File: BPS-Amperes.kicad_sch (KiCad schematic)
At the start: 46 parts, among them J1 ShuntConn, J2 LeaderConn, J3 Conn_01x04, U1 INA186A3IDDFT, U2 RO-123.3S_HP, U3 LTC6820, U4 HX1188FNL, U5 REF1930AIDDCT, U6 LTC2315, U7 OPA2196

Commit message: Minor fixing
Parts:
- D1: symbol Device:LED_ALT -> Device:LED
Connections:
- net GND: now also D1.1 (K)
- net at R2.2: now also D1.2 (A)
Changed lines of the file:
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@@
     (pin "2")
   )
-  (symbol (lib_id "Device:LED_ALT") (at 121.92 57.15 90) (unit 1)
+  (symbol (lib_id "Device:LED") (at 121.92 57.15 90) (unit 1)
     (in_bom yes) (on_board yes)
     (property "Reference" "D1" (id 0) (at 124.9172 56.1594 90)
@@
       (effects (font (size 1.27 1.27)) hide)
     )
+    (pin "1")
+    (pin "2")
   )
   (symbol (lib_id "power:GNDPWR") (at 40.64 60.96 0) (unit 1)

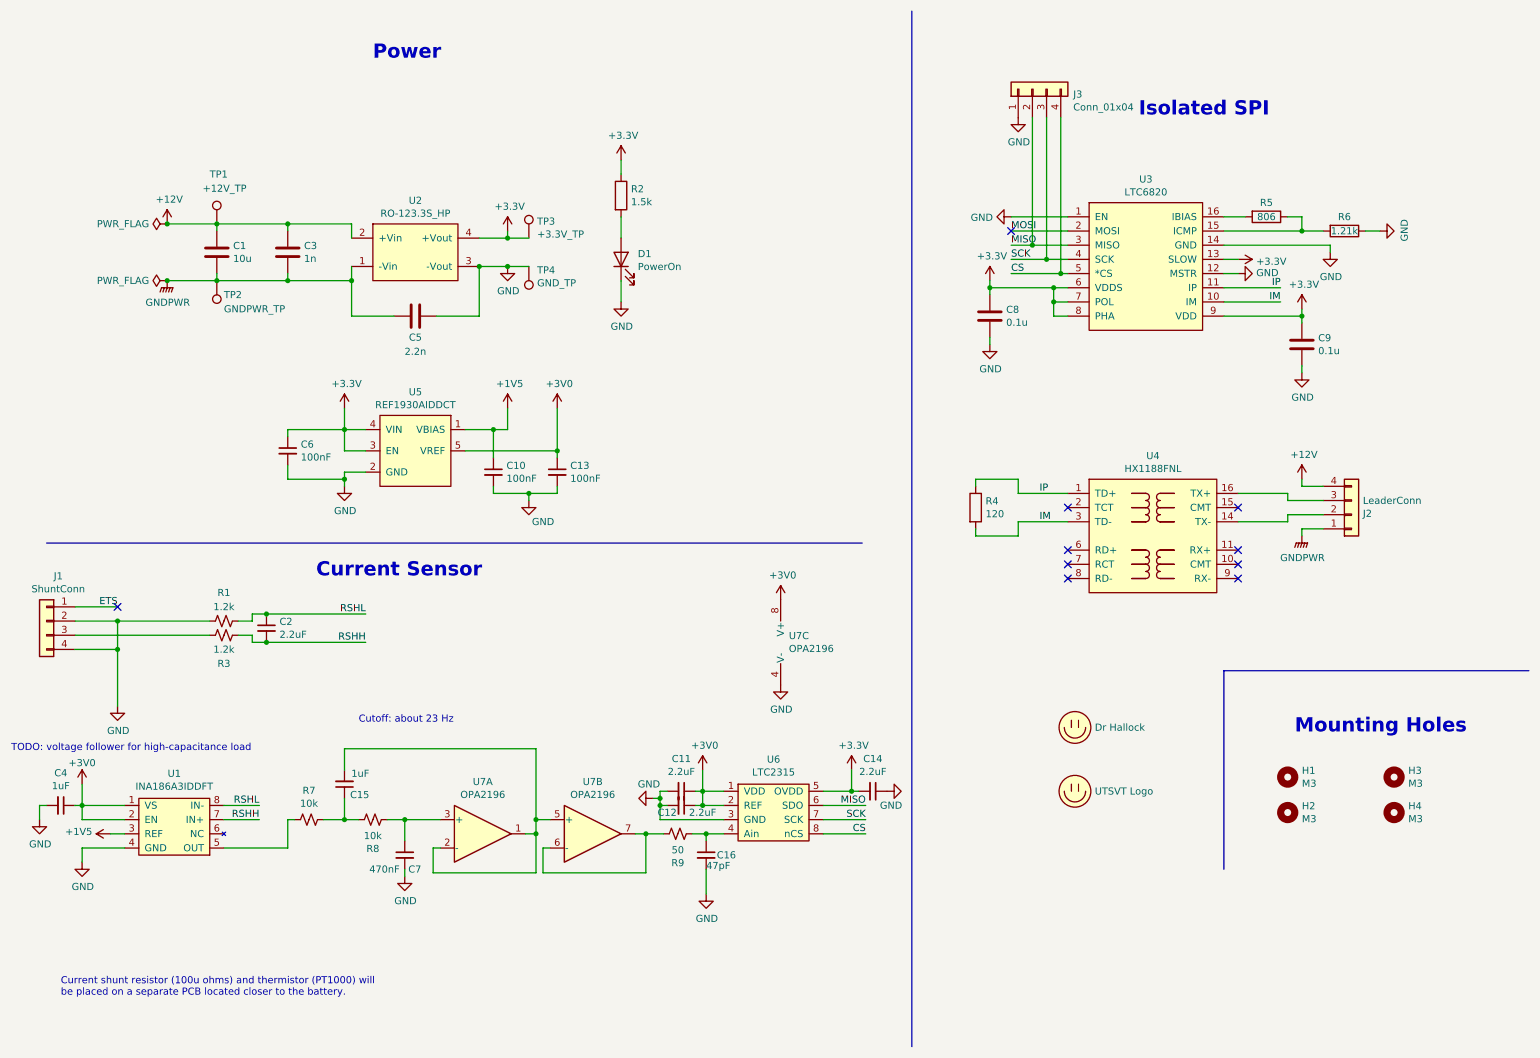
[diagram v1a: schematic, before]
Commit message: emi + reverse polarity + analog overvolt protection
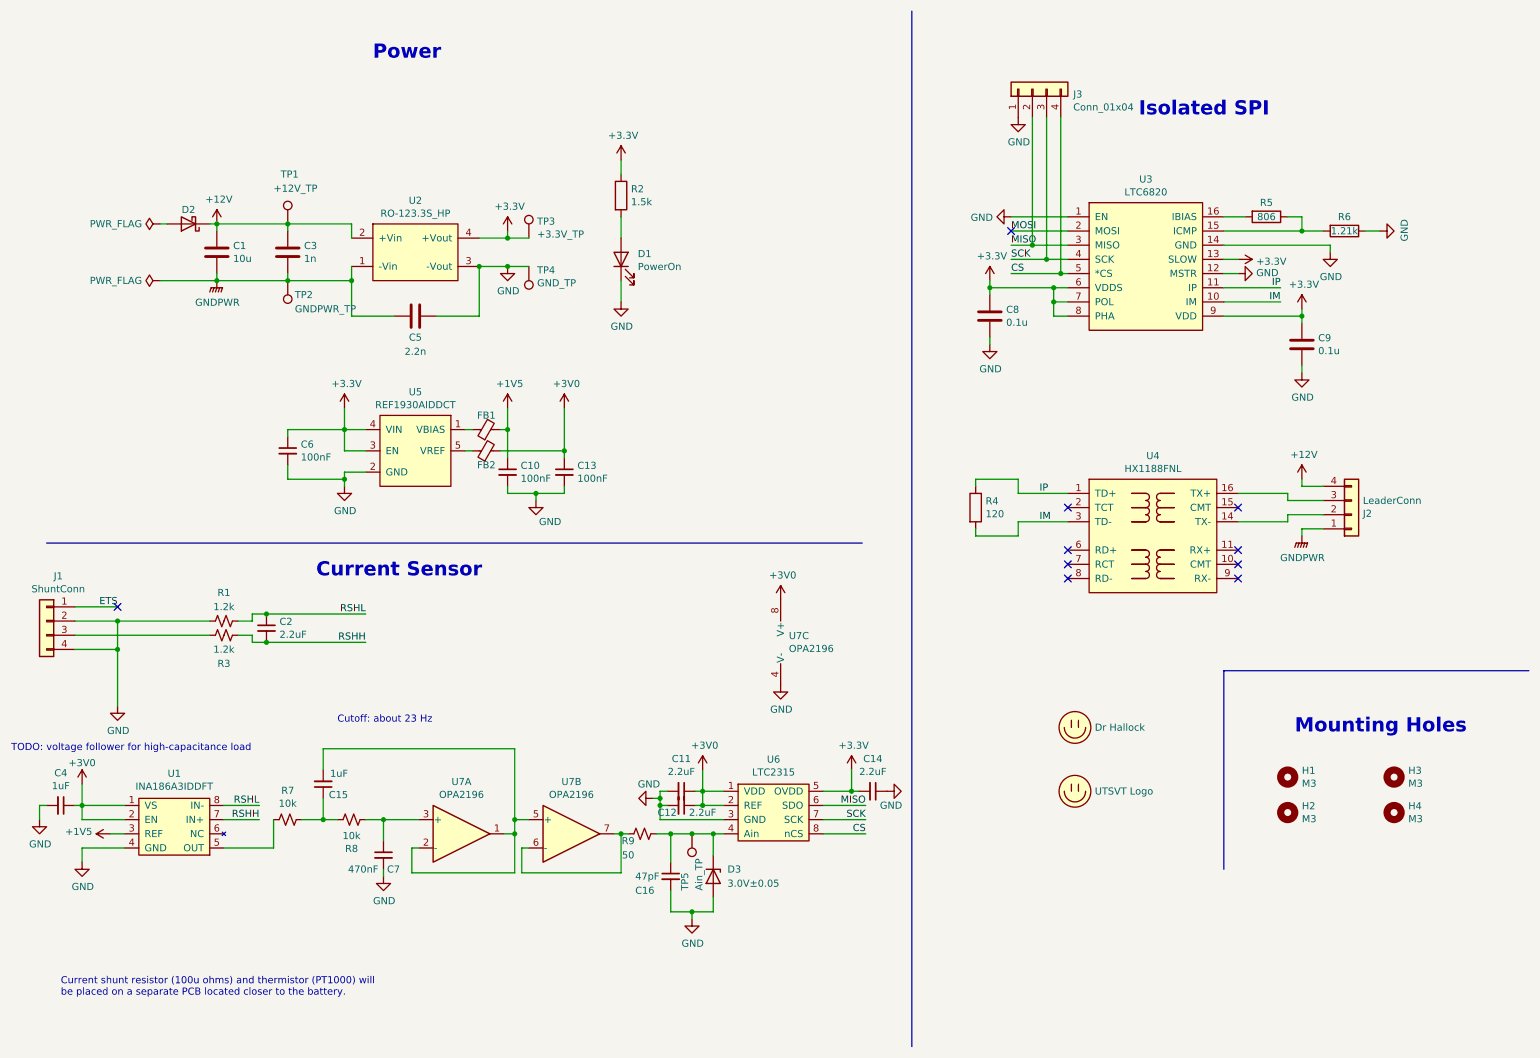
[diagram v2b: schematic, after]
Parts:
- added D2: D_Schottky, symbol Device:D_Schottky
- added D3: 3.0V±0.05, symbol Device:D_Zener
- added FB1, FB2: FerriteBead_Small, symbol Device:FerriteBead_Small
- added TP5: Ain_TP, symbol Connector:TestPoint
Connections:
- net +12V: now also D2.1 (K)
- net +1V5: now also FB1.2; no longer U5.1 (VBIAS)
- net +3V0: now also FB2.2; no longer U5.5 (VREF)
- net GND: now also D3.2 (A)
- net at C16.1, R9.2, U6.4 (Ain): now also D3.1 (K), TP5.1
- new net: FB1.1, U5.1 (VBIAS)
- new net: FB2.1, U5.5 (VREF)
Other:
- moved on the sheet: C10, C13, C15, C16, C7, R7, R8, R9, TP1, TP2, U7A, U7B

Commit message: hat connector
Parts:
- J1: symbol Connector_Generic:Conn_01x04 -> Connector_Generic:Conn_01x05
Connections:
- net +3V3: now also J1.4 (Pin_4)
- net GND: now also J1.5 (Pin_5); no longer J1.4 (Pin_4)

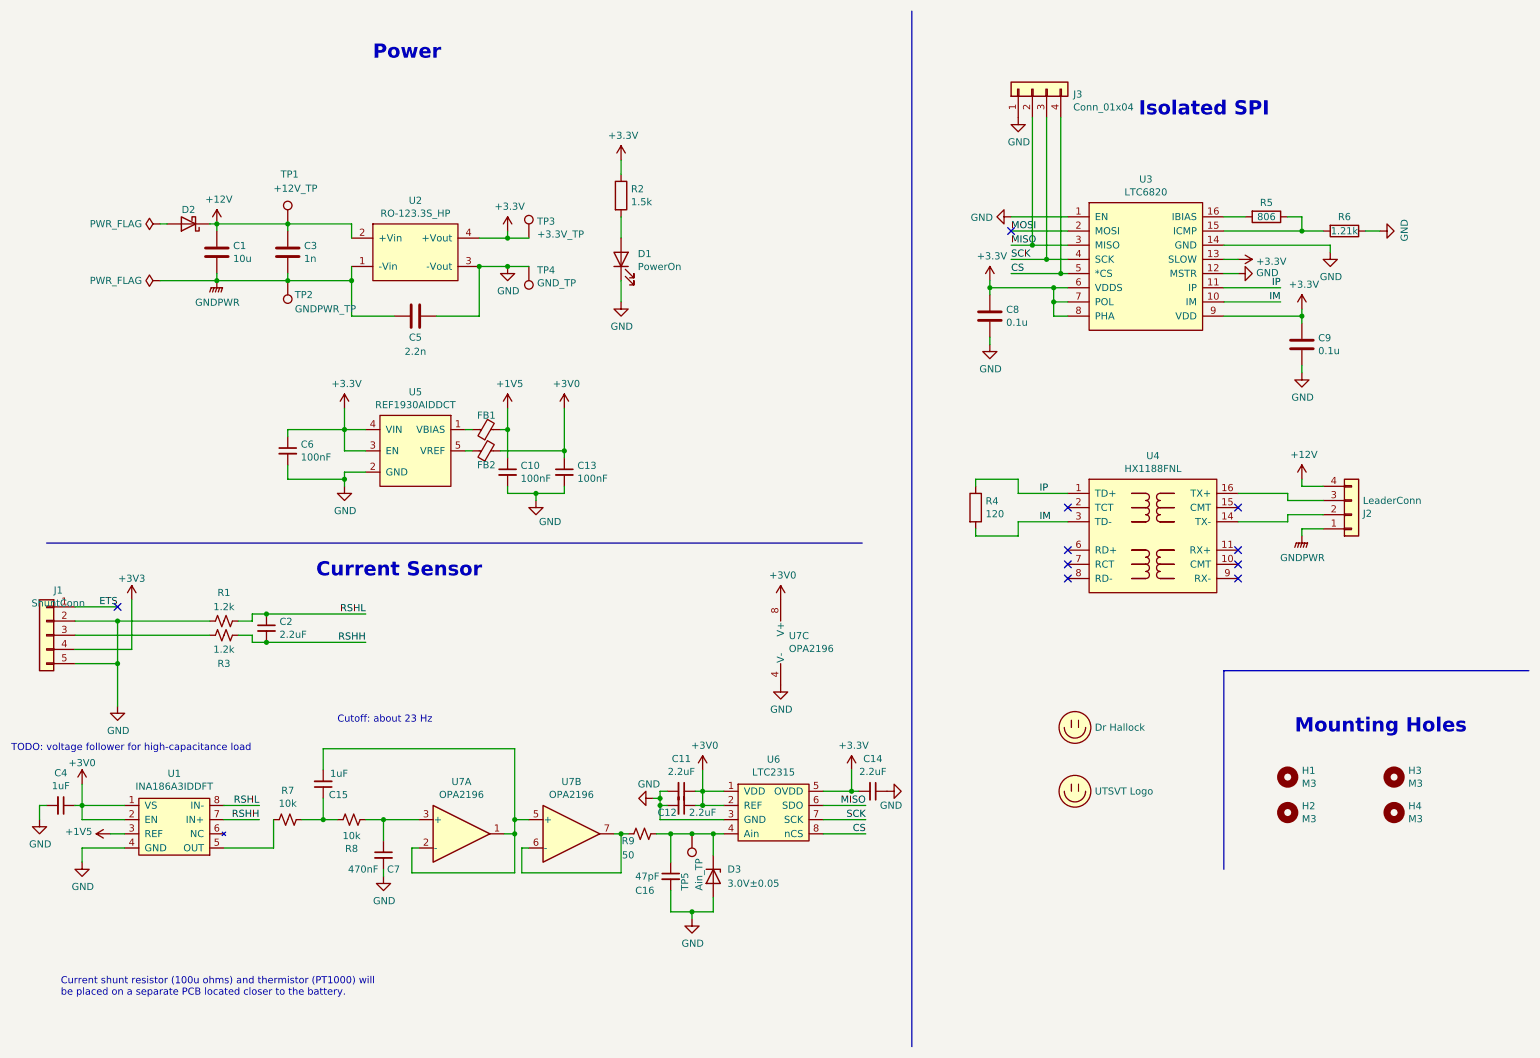
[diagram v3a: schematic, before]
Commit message: more bypass caps and other fixes
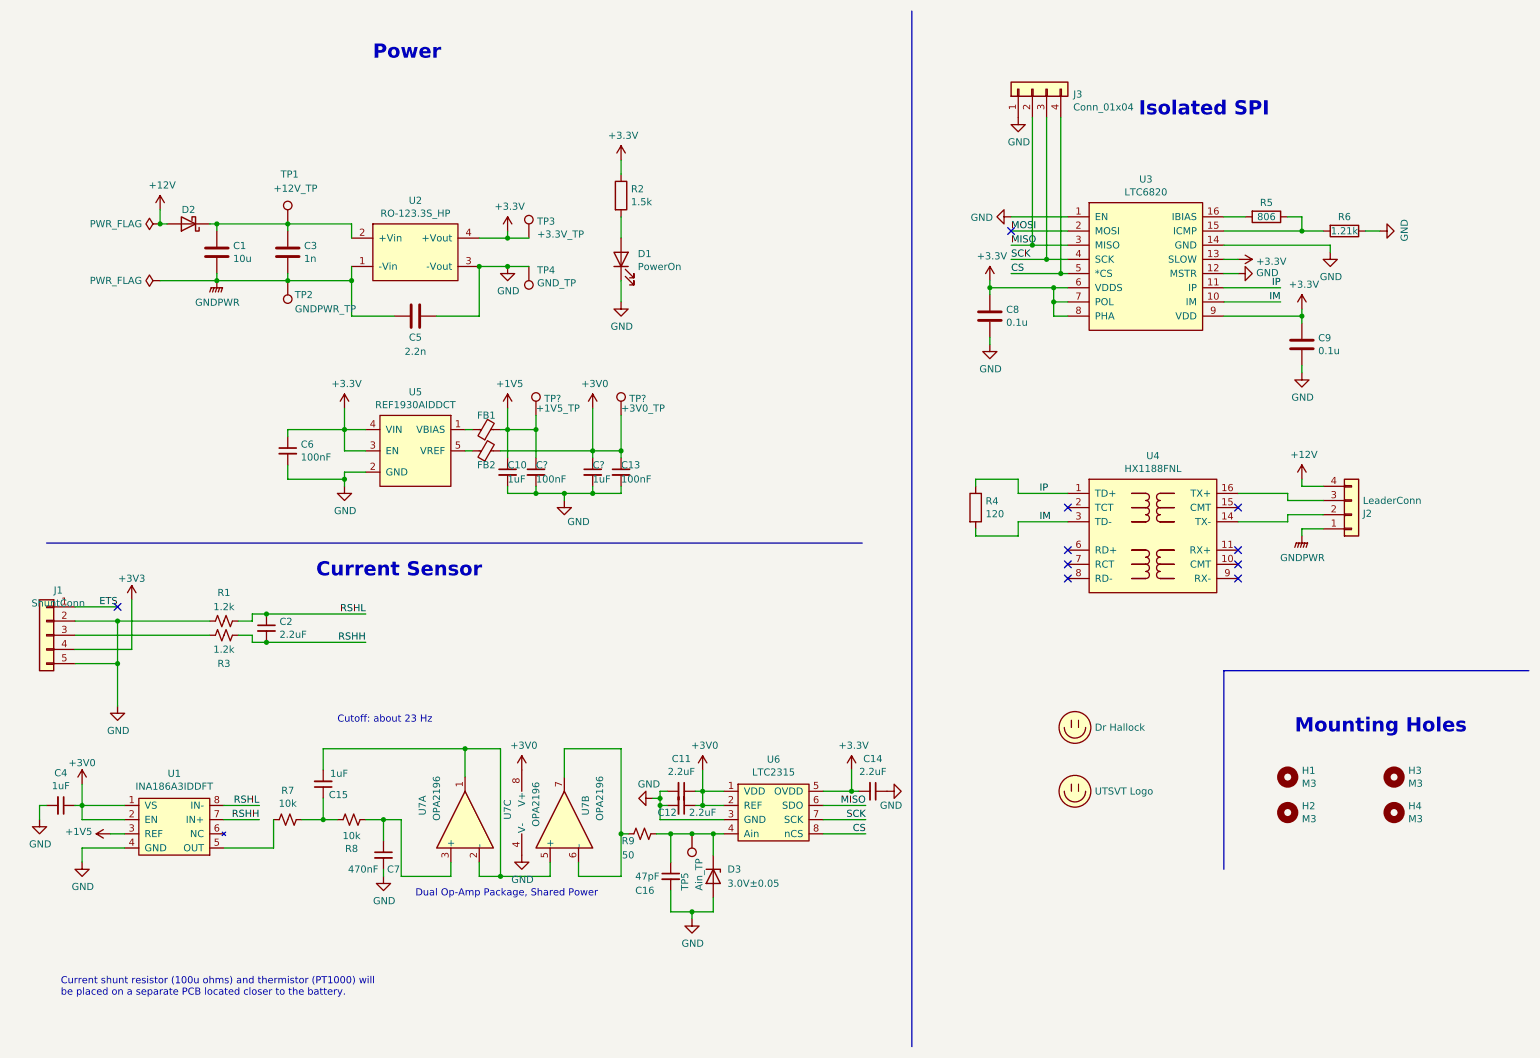
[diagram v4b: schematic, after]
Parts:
- added C?: 100nF, Capacitor_SMD:C_0805_2012Metric, symbol Device:C_Small
- added C?: 1uF, Capacitor_SMD:C_0805_2012Metric, symbol Device:C_Small
- added TP?: +1V5_TP, TestPoint:TestPoint_Keystone_5005-5009_Compact, symbol Connector:TestPoint
- added TP?: +3V0_TP, TestPoint:TestPoint_Keystone_5005-5009_Compact, symbol Connector:TestPoint
- C10: value 100nF -> 1uF
- FB1, FB2: footprint (none) -> Inductor_SMD:L_0805_2012Metric
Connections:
- net +12V: now also D2.2 (A); no longer C1.1, C3.1, D2.1 (K), TP1.1, U2.2 (+Vin)
- net +1V5: now also C?.1, TP?.1
- net +3V0: now also C?.1, TP?.1
- net GND: now also C?.2, C?.2
- new net: C1.1, C3.1, D2.1 (K), TP1.1, U2.2 (+Vin)
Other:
- note added: "Dual Op-Amp Package, Shared Power"
- note removed: "TODO: voltage follower for high-capacitance load"
- moved on the sheet: C13, U7A, U7B, U7C

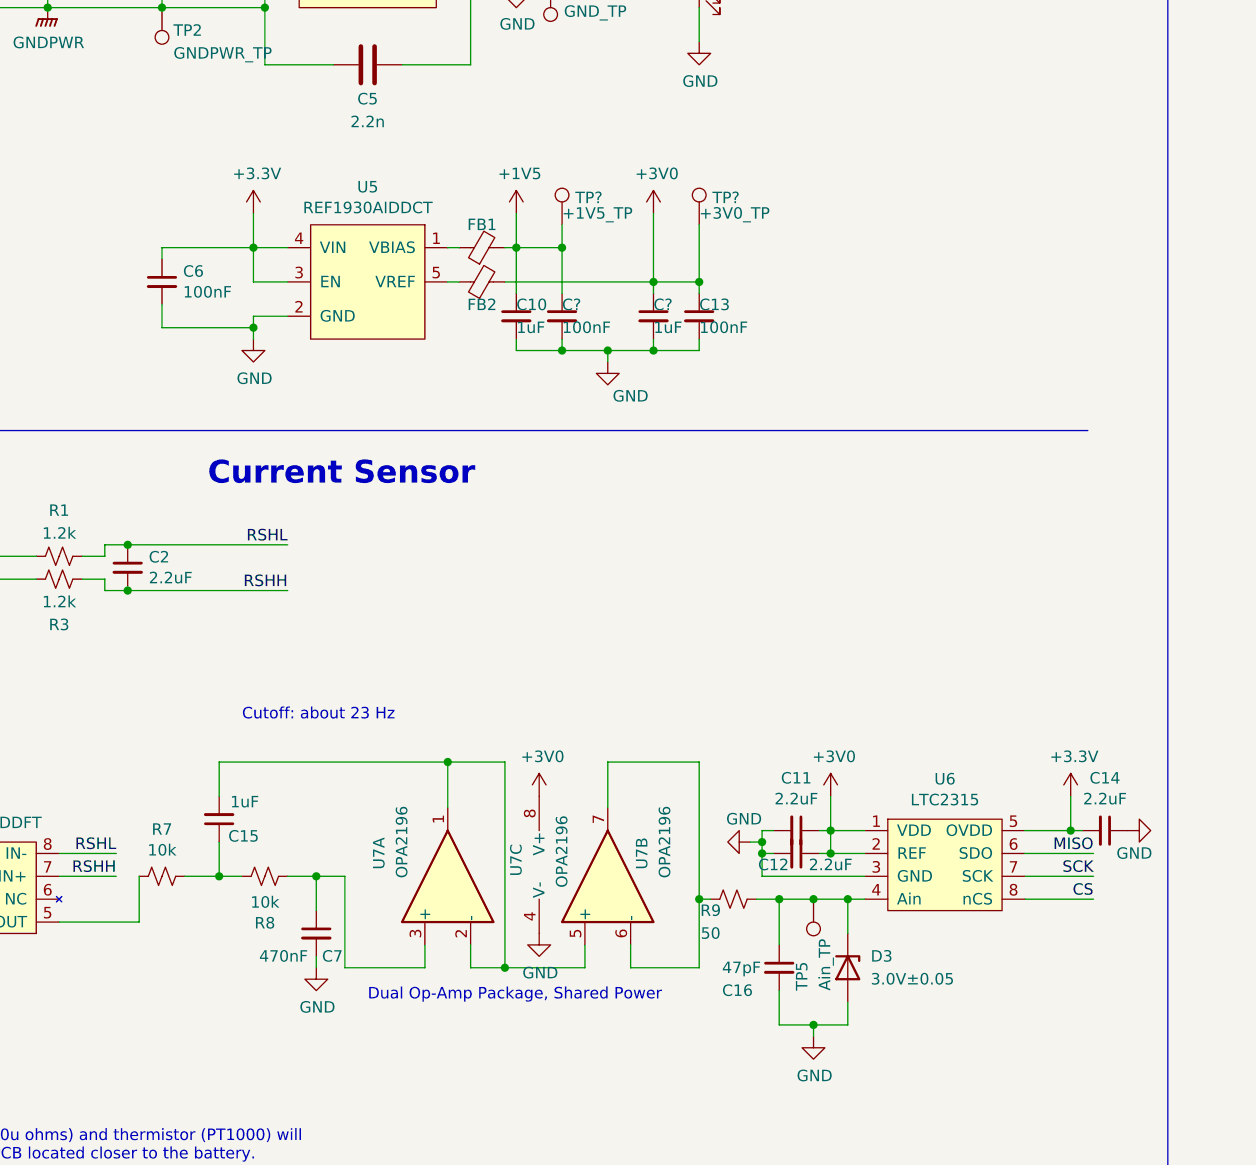
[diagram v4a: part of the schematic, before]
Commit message: make a little easier on the eyes
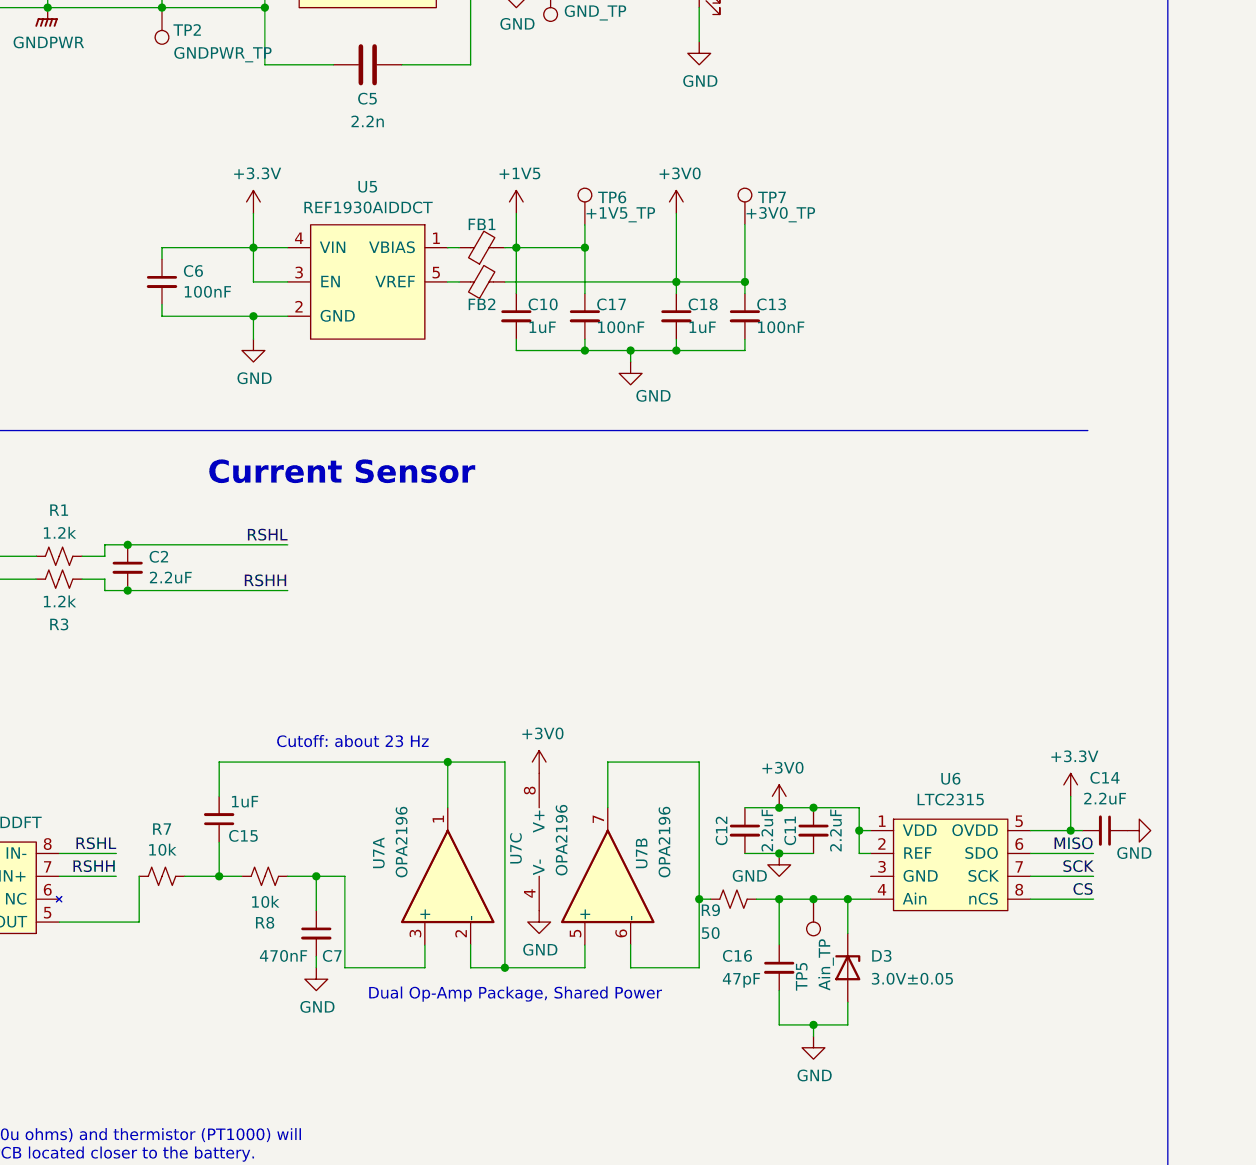
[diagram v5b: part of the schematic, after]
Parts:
- gave numbers to parts that had none: 4
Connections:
- net GND: no longer U6.3 (GND)
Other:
- moved on the sheet: C11, C12, C13, C17, C18, TP6, TP7, U6, U7C
